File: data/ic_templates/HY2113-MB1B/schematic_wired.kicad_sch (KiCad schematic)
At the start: 12 parts, among them J1 B+/B-/P+/P-, Q1 FS8205A, U1 HY2113-MB1B

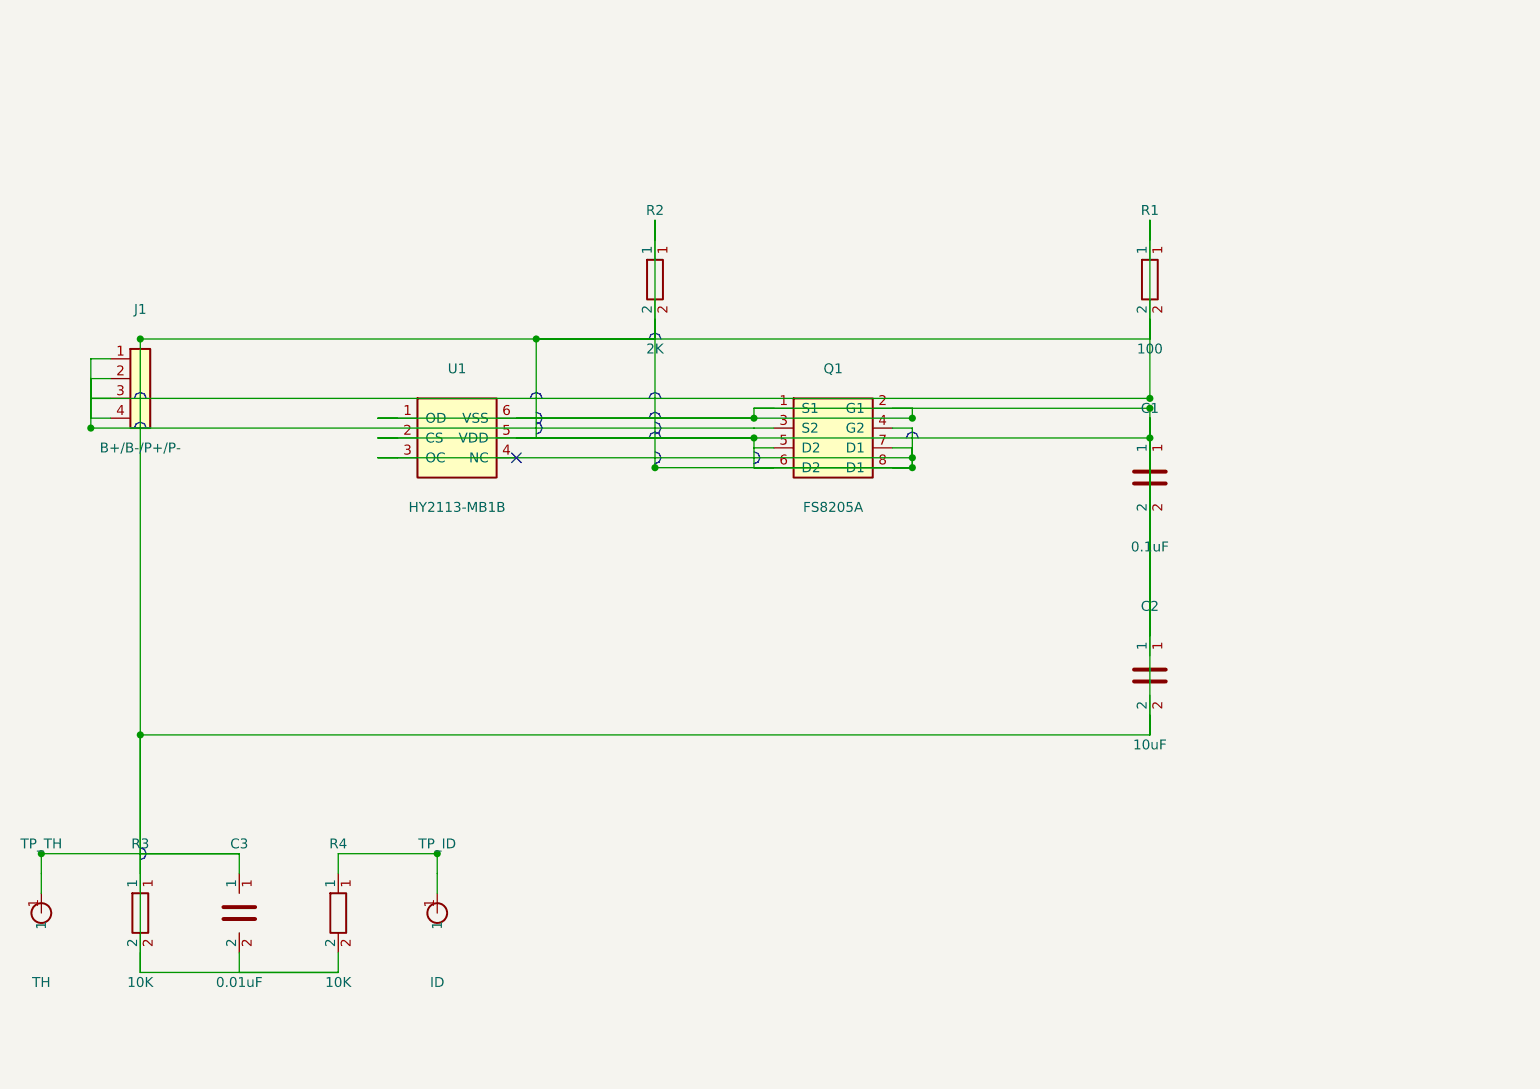
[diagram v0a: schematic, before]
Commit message: fix: 修复黑框检测阈值策略 — 固定阈值70改为 Otsu+Adaptive 混合阈值
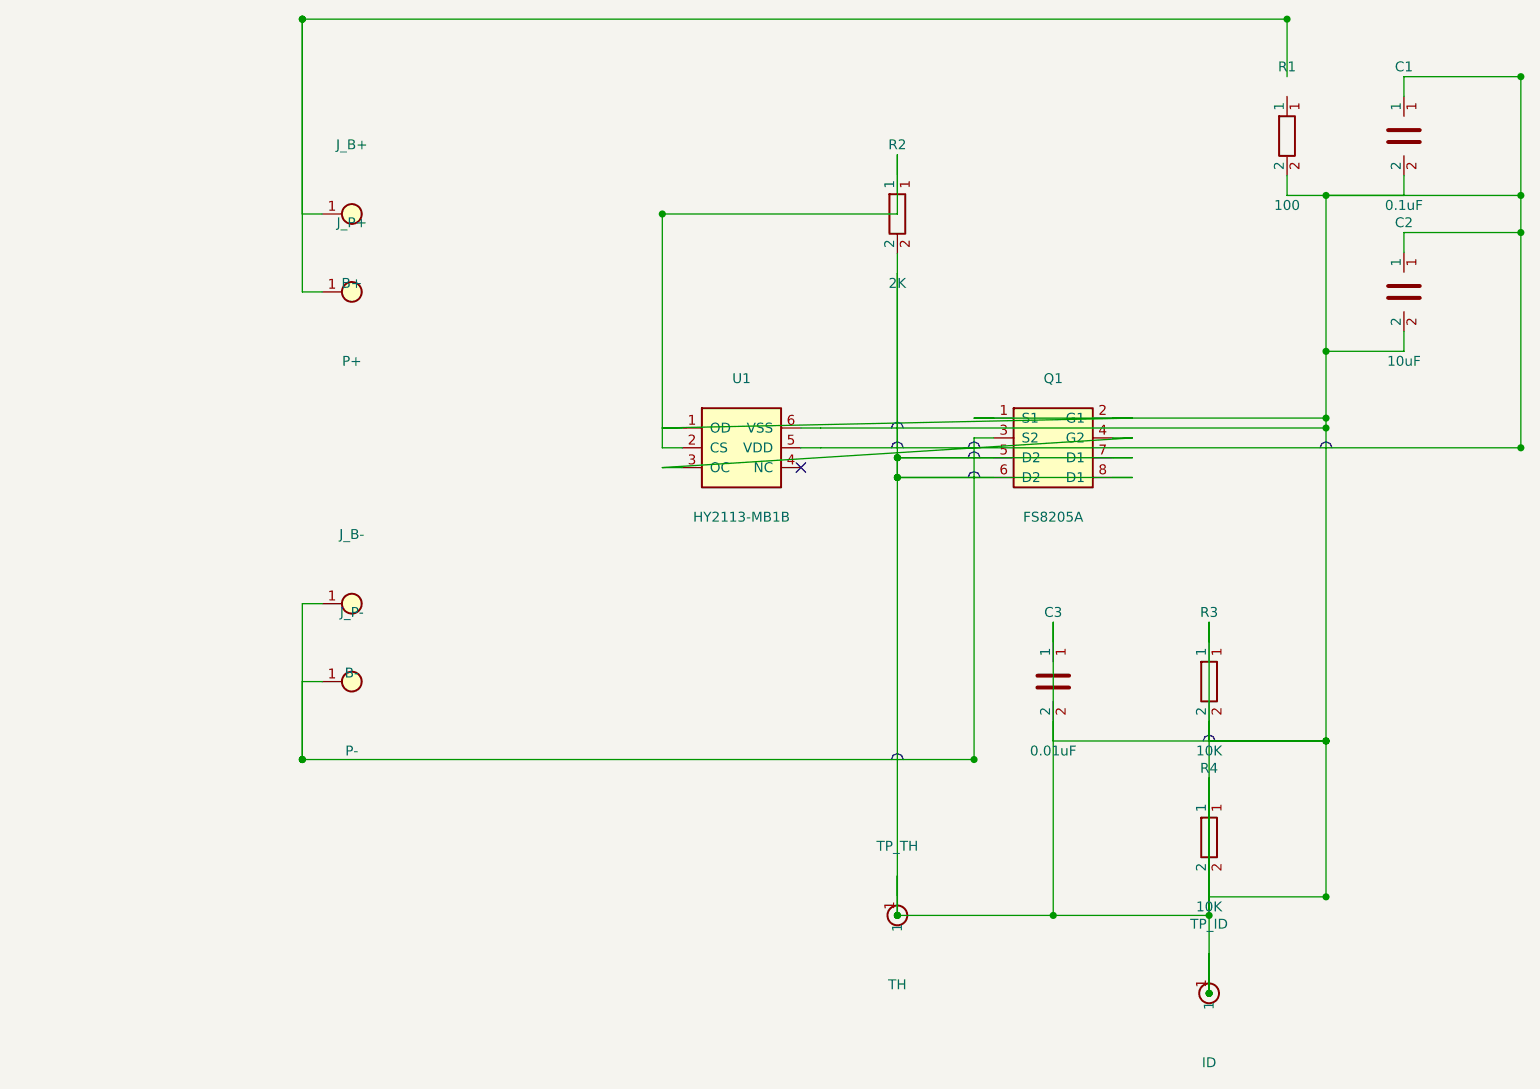
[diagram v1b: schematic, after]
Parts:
- removed J1: B+/B-/P+/P-, Connector_PinHeader_2.54mm:PinHeader_1x04_P2.54mm_Vertical, symbol battery_protection:Conn_01x04
- added J_B+: B+, Connector_PinHeader_2.54mm:PinHeader_1x01_P2.54mm_Vertical, symbol battery_protection:Conn_01x01
- added J_B-: B-, Connector_PinHeader_2.54mm:PinHeader_1x01_P2.54mm_Vertical, symbol battery_protection:Conn_01x01
- added J_P+: P+, Connector_PinHeader_2.54mm:PinHeader_1x01_P2.54mm_Vertical, symbol battery_protection:Conn_01x01
- added J_P-: P-, Connector_PinHeader_2.54mm:PinHeader_1x01_P2.54mm_Vertical, symbol battery_protection:Conn_01x01
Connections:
- net at C1.1, C1.2, C2.1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: now also R4.1, TP_ID.1; no longer Q1.3 (S2), Q1.4 (G2), R1.1, R2.1, U1.2 (CS), U1.3 (OC)
- new net: R2.1, U1.2 (CS)
- new net: Q1.4 (G2), U1.3 (OC)
- new net: J_B-.1, J_P-.1, Q1.3 (S2)
- new net: J_B+.1, J_P+.1
